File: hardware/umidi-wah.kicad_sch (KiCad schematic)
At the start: 34 parts, among them J1 Conn_01x02, J10 Conn_02x05_Odd_Even, J2 Conn_01x02, J3 Conn_02x05_Odd_Even, J4 Conn_01x02, J5 Input, J6 Output, J7 Conn_02x05_Odd_Even, J8 Conn_02x05_Odd_Even, J9 Conn_02x05_Odd_Even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

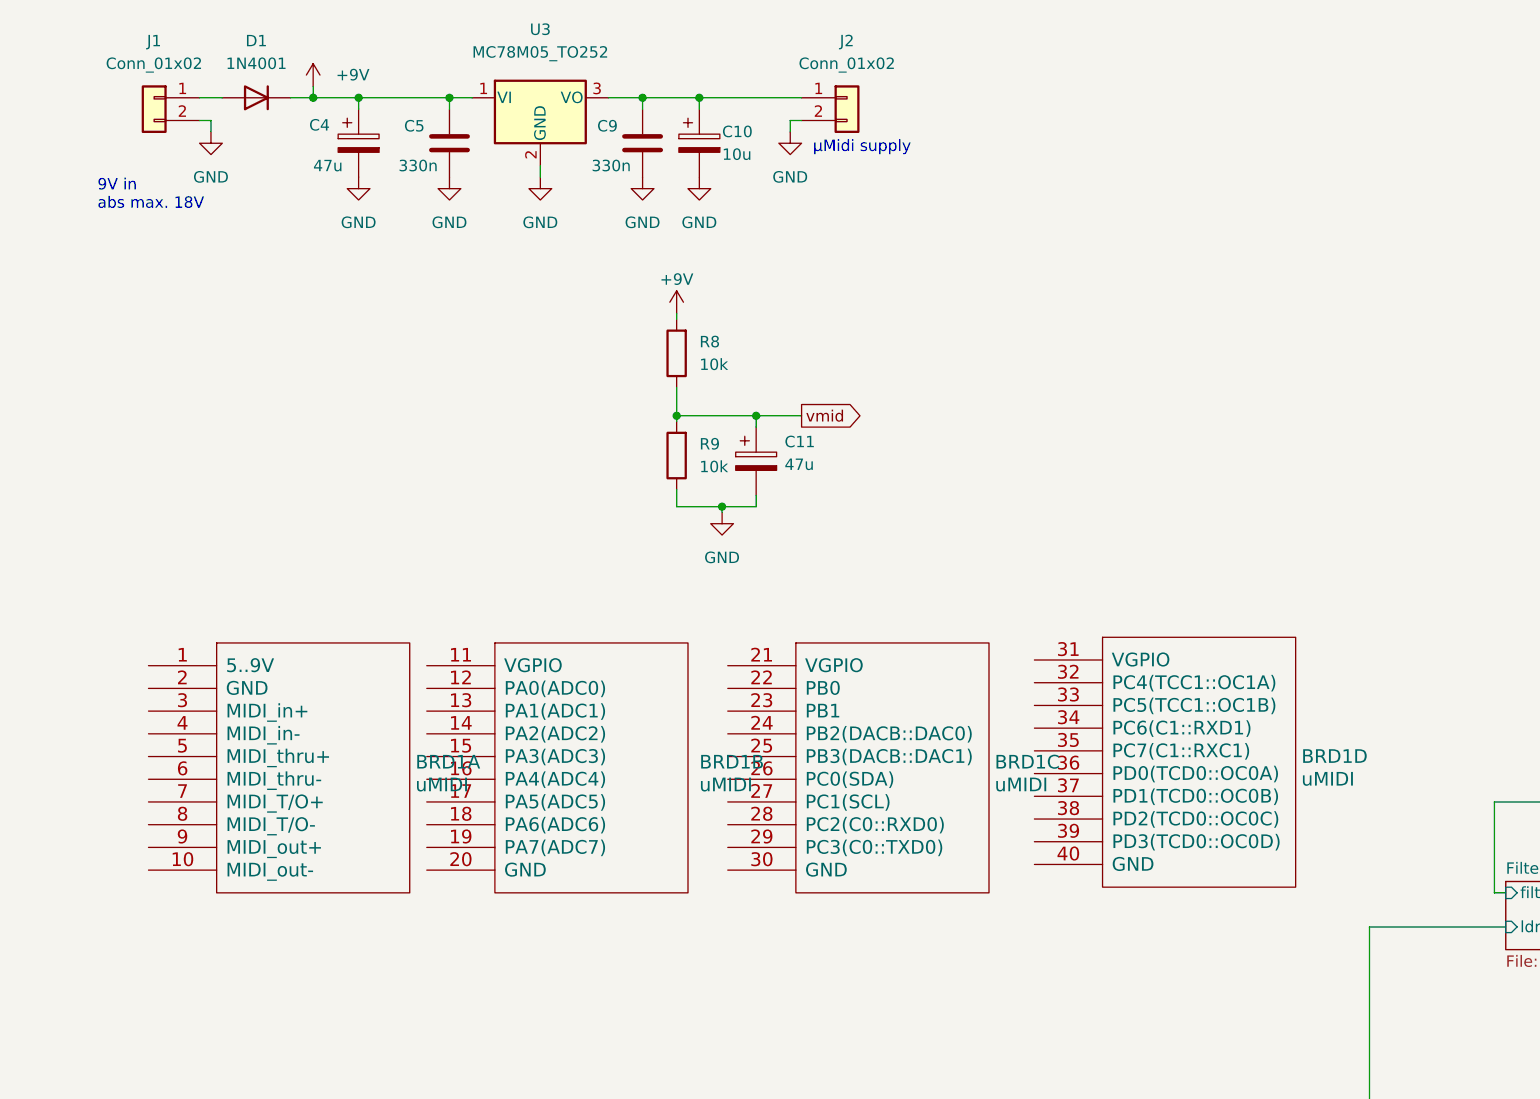
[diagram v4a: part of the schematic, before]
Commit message: Connect power to uMidi module
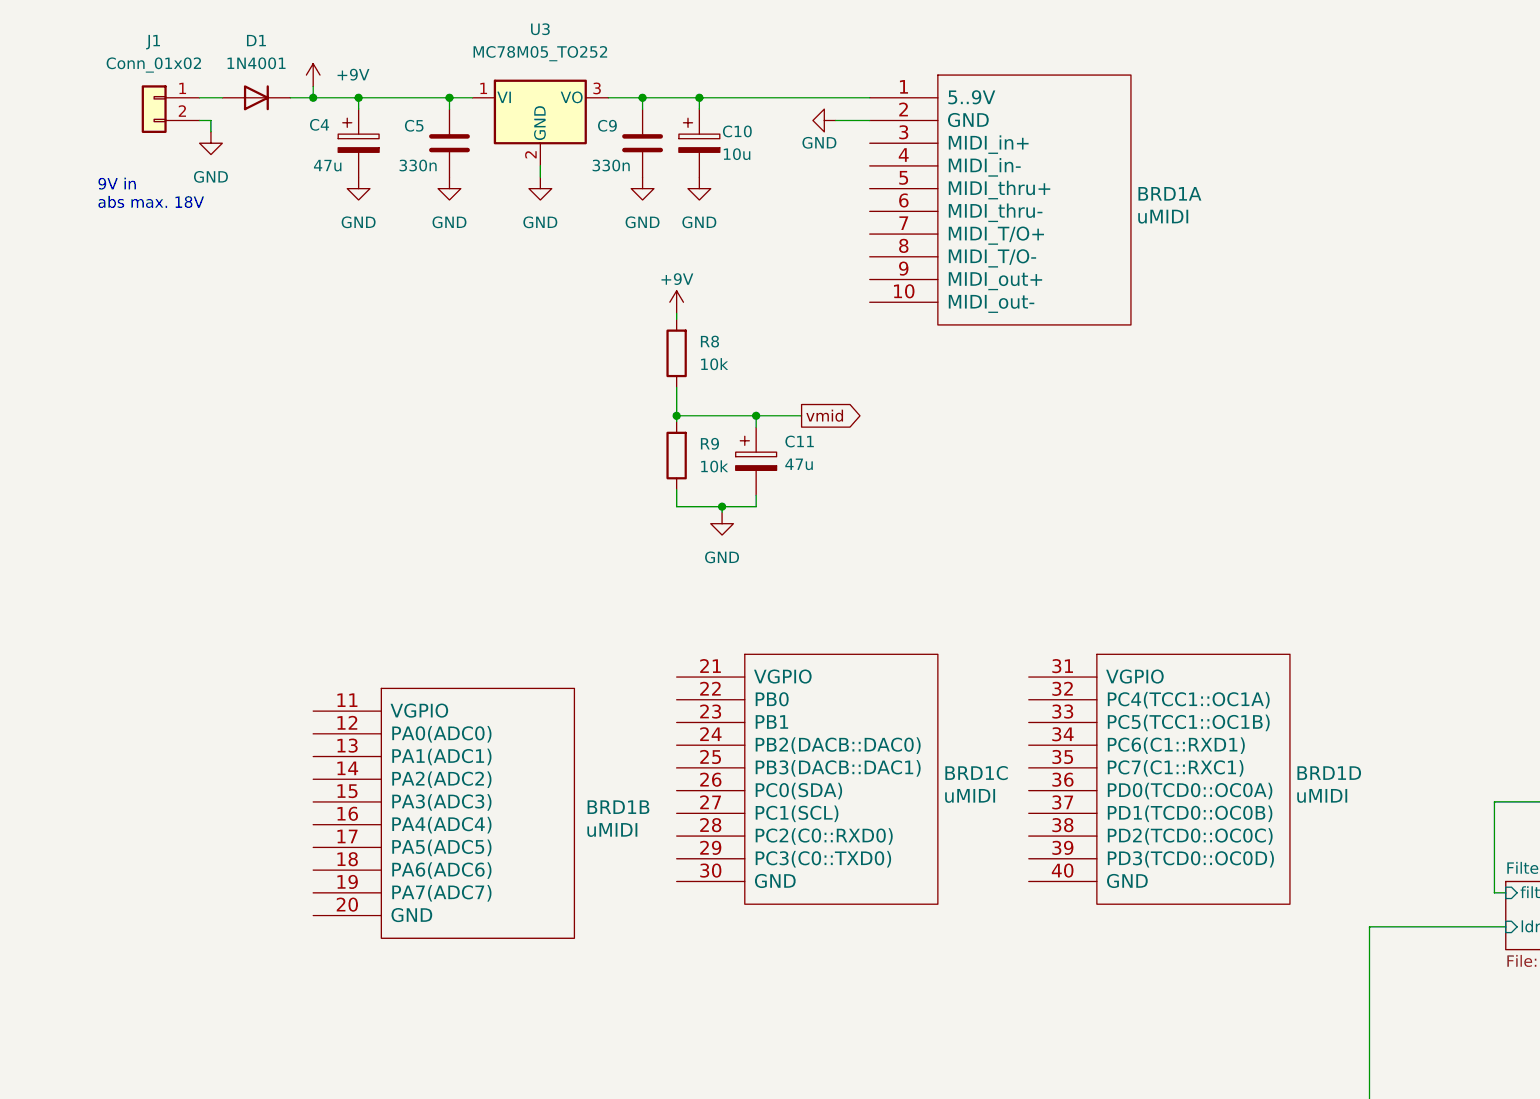
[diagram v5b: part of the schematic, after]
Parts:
- removed J2: Conn_01x02, Connector_Wire:SolderWire-1sqmm_1x02_P5.4mm_D1.4mm_OD2.7mm, symbol Connector_Generic:Conn_01x02
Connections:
- net GND: now also BRD1.2 (GND)
- net at C10.1, C9.1, U3.3 (VO): now also BRD1.1 (5..9V)
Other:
- note removed: "μMidi supply"
- moved on the sheet: BRD1A, BRD1B, BRD1C, BRD1D
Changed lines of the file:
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@@
-    (stroke (width 0) (type default))
-  )
-  (wire (pts (xy 99.06 27.94) (xy 97.79 27.94))
     (stroke (width 0) (type default))
   )
@@
     (stroke (width 0) (type default))
   )
-  (wire (pts (xy 87.63 25.4) (xy 99.06 25.4))
+  (wire (pts (xy 87.63 25.4) (xy 106.68 25.4))
     (stroke (width 0) (type default))
   )
@@
     (stroke (width 0) (type default))
   )
-  (wire (pts (xy 97.79 27.94) (xy 97.79 29.21))
-    (stroke (width 0) (type default))
-  )
   (wire (pts (xy 86.36 162.56) (xy 85.09 162.56))
     (stroke (width 0) (type default))
@@
   )
   (wire (pts (xy 87.63 25.4) (xy 87.63 26.67))
+    (stroke (width 0) (type default))
+  )
+  (wire (pts (xy 102.87 27.94) (xy 106.68 27.94))
     (stroke (width 0) (type default))
   )
@@
   (text "Three 10-pin sockets placed on bottom to attach uMidi board.\nGPIO1 and 2 are passed through to optional 10-pin headers.\n"
     (at 115.57 142.24 0)
-    (effects (font (size 1.27 1.27)) (justify left bottom))
-  )
-  (text "μMidi supply" (at 100.33 31.75 0)
     (effects (font (size 1.27 1.27)) (justify left bottom))
   )
@@
     )
   )
-  (symbol (lib_id "power:GND") (at 97.79 29.21 0) (mirror y) (unit 1)
-    (in_bom yes) (on_board yes) (dnp no) (fields_autoplaced)
-    (property "Reference" "#PWR0136" (at 97.79 35.56 0)
-      (effects (font (size 1.27 1.27)) hide)
-    )
-    (property "Value" "GND" (at 97.79 34.29 0)
-      (effects (font (size 1.27 1.27)))
-    )
-    (property "Footprint" "" (at 97.79 29.21 0)
-      (effects (font (size 1.27 1.27)) hide)
-    )
-    (property "Datasheet" "" (at 97.79 29.21 0)
+  (symbol (lib_id "power:GND") (at 102.87 27.94 270) (mirror x) (unit 1)
+    (in_bom yes) (on_board yes) (dnp no)
+    (property "Reference" "#PWR0136" (at 96.52 27.94 0)
+      (effects (font (size 1.27 1.27)) hide)
+    )
+    (property "Value" "GND" (at 99.06 30.48 90)
+      (effects (font (size 1.27 1.27)) (justify left))
+    )
+    (property "Footprint" "" (at 102.87 27.94 0)
+      (effects (font (size 1.27 1.27)) hide)
+    )
+    (property "Datasheet" "" (at 102.87 27.94 0)
       (effects (font (size 1.27 1.27)) hide)
     )
@@
     )
   )
-  (symbol (lib_id "umidi-wah:uMIDI") (at 108.585 100.33 0) (unit 3)
-    (in_bom yes) (on_board yes) (dnp no) (fields_autoplaced)
-    (property "Reference" "BRD1" (at 120.65 99.695 0)
+  (symbol (lib_id "umidi-wah:uMIDI") (at 102.87 101.6 0) (unit 3)
+    (in_bom yes) (on_board yes) (dnp no) (fields_autoplaced)
+    (property "Reference" "BRD1" (at 114.935 100.965 0)
       (effects (font (size 1.524 1.524)) (justify left))
     )
-    (property "Value" "uMIDI" (at 120.65 102.235 0)
+    (property "Value" "uMIDI" (at 114.935 103.505 0)
       (effects (font (size 1.524 1.524)) (justify left))
     )
-    (property "Footprint" "uMidi-wah:uMIDI_faceup" (at 103.505 100.33 0)
+    (property "Footprint" "uMidi-wah:uMIDI_faceup" (at 97.79 101.6 0)
       (effects (font (size 1.524 1.524)) hide)
     )
-    (property "Datasheet" "" (at 103.505 100.33 0)
+    (property "Datasheet" "" (at 97.79 101.6 0)
       (effects (font (size 1.524 1.524)))
     )
@@
     )
   )
-  (symbol (lib_id "Connector_Generic:Conn_01x02") (at 104.14 25.4 0) (unit 1)
-    (in_bom yes) (on_board yes) (dnp no) (fields_autoplaced)
-    (property "Reference" "J2" (at 104.14 19.05 0)
-      (effects (font (size 1.27 1.27)))
-    )
-    (property "Value" "Conn_01x02" (at 104.14 21.59 0)
-      (effects (font (size 1.27 1.27)))
-    )
-    (property "Footprint" "Connector_Wire:SolderWire-1sqmm_1x02_P5.4mm_D1.4mm_OD2.7mm" (at 104.14 25.4 0)
-      (effects (font (size 1.27 1.27)) hide)
-    )
-    (property "Datasheet" "~" (at 104.14 25.4 0)
-      (effects (font (size 1.27 1.27)) hide)
-    )
-    (pin "1")
-    (pin "2")
-    (instances
-      (project "umidi-wah"
-        (path "/8f66db7e-cf06-4b3a-905e-a75646e85499"
-          (reference "J2") (unit 1)
-        )
-      )
-    )
-  )
   (symbol (lib_id "Device:Q_NPN_ECB") (at 255.27 152.4 0) (unit 1)
     (in_bom yes) (on_board yes) (dnp no) (fields_autoplaced)
@@
     )
   )
-  (symbol (lib_id "umidi-wah:uMIDI") (at 43.815 100.33 0) (unit 1)
-    (in_bom yes) (on_board yes) (dnp no) (fields_autoplaced)
-    (property "Reference" "BRD1" (at 55.88 99.695 0)
+  (symbol (lib_id "umidi-wah:uMIDI") (at 124.46 36.83 0) (unit 1)
+    (in_bom yes) (on_board yes) (dnp no) (fields_autoplaced)
+    (property "Reference" "BRD1" (at 136.525 36.195 0)
       (effects (font (size 1.524 1.524)) (justify left))
     )
-    (property "Value" "uMIDI" (at 55.88 102.235 0)
+    (property "Value" "uMIDI" (at 136.525 38.735 0)
       (effects (font (size 1.524 1.524)) (justify left))
     )
-    (property "Footprint" "uMidi-wah:uMIDI_faceup" (at 38.735 100.33 0)
+    (property "Footprint" "uMidi-wah:uMIDI_faceup" (at 119.38 36.83 0)
       (effects (font (size 1.524 1.524)) hide)
     )
-    (property "Datasheet" "" (at 38.735 100.33 0)
+    (property "Datasheet" "" (at 119.38 36.83 0)
       (effects (font (size 1.524 1.524)))
     )
@@
     )
   )
-  (symbol (lib_id "umidi-wah:uMIDI") (at 142.875 99.695 0) (unit 4)
-    (in_bom yes) (on_board yes) (dnp no) (fields_autoplaced)
-    (property "Reference" "BRD1" (at 154.94 99.06 0)
+  (symbol (lib_id "umidi-wah:uMIDI") (at 142.24 101.6 0) (unit 4)
+    (in_bom yes) (on_board yes) (dnp no) (fields_autoplaced)
+    (property "Reference" "BRD1" (at 154.305 100.965 0)
       (effects (font (size 1.524 1.524)) (justify left))
     )
-    (property "Value" "uMIDI" (at 154.94 101.6 0)
+    (property "Value" "uMIDI" (at 154.305 103.505 0)
       (effects (font (size 1.524 1.524)) (justify left))
     )
-    (property "Footprint" "uMidi-wah:uMIDI_faceup" (at 137.795 99.695 0)
+    (property "Footprint" "uMidi-wah:uMIDI_faceup" (at 137.16 101.6 0)
       (effects (font (size 1.524 1.524)) hide)
     )
-    (property "Datasheet" "" (at 137.795 99.695 0)
+    (property "Datasheet" "" (at 137.16 101.6 0)
       (effects (font (size 1.524 1.524)))
     )
@@
     )
   )
-  (symbol (lib_id "umidi-wah:uMIDI") (at 74.93 100.33 0) (unit 2)
-    (in_bom yes) (on_board yes) (dnp no) (fields_autoplaced)
-    (property "Reference" "BRD1" (at 87.63 99.695 0)
+  (symbol (lib_id "umidi-wah:uMIDI") (at 62.23 105.41 0) (unit 2)
+    (in_bom yes) (on_board yes) (dnp no) (fields_autoplaced)
+    (property "Reference" "BRD1" (at 74.93 104.775 0)
       (effects (font (size 1.524 1.524)) (justify left))
     )
-    (property "Value" "uMIDI" (at 87.63 102.235 0)
+    (property "Value" "uMIDI" (at 74.93 107.315 0)
       (effects (font (size 1.524 1.524)) (justify left))
     )
-    (property "Footprint" "uMidi-wah:uMIDI_faceup" (at 69.85 100.33 0)
+    (property "Footprint" "uMidi-wah:uMIDI_faceup" (at 57.15 105.41 0)
       (effects (font (size 1.524 1.524)) hide)
     )
-    (property "Datasheet" "" (at 69.85 100.33 0)
+    (property "Datasheet" "" (at 57.15 105.41 0)
       (effects (font (size 1.524 1.524)))
     )
